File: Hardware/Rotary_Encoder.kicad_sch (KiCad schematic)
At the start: 10 parts, among them SW1 PEC12R-4115F-S0012

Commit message: Clean up custom KiCad libraries
- Clean up the directory structure for KiCad custom libraries.
- Fix paths in KiCad schematic and pcb for symbols, footprints, and
3d models for custom libraries.
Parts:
- SW1: footprint Libs:PEC12R-4115F-S0012 -> Encoder:PEC12R-4115F-S0012
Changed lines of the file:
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@@
   (title_block
     (title "Musical Doorbell")
-    (date "2022-01-06")
-    (rev "B")
+    (date "2022-01-09")
+    (rev "A")
     (company "Michael Lazernik")
   )
@@
     (property "Reference" "SW1" (id 0) (at 143.51 87.1982 0))
     (property "Value" "PEC12R-4115F-S0012" (id 1) (at 143.51 89.5096 0))
-    (property "Footprint" "Libs:PEC12R-4115F-S0012" (id 2) (at 139.7 92.456 0)
+    (property "Footprint" "Encoder:PEC12R-4115F-S0012" (id 2) (at 139.7 92.456 0)
       (effects (font (size 1.27 1.27)) hide)
     )

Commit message: Cleanup custom KiCad libraries
- Delete unneeded/unused files
- Cleanup symbol library files for custom libraries
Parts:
- SW1: symbol PEC12R-4115F-S0012:PEC12R-4115F-S0012 -> Doorbell_Encoder:PEC12R-4115F-S0012
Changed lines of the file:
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@@
     (effects (font (size 1.27 1.27)) (justify left))
   )
-  (symbol (lib_id "PEC12R-4115F-S0012:PEC12R-4115F-S0012") (at 143.51 96.52 0) (unit 1)
+  (symbol (lib_id "Doorbell_Encoder:PEC12R-4115F-S0012") (at 143.51 96.52 0) (unit 1)
     (in_bom yes) (on_board yes)
     (property "Reference" "SW1" (id 0) (at 143.51 87.1982 0))

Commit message: Switch to local libraries for KiCad schematic
- Move all KiCad schematic symbols into local libraries
- Fix KiCad schematic library links to point to local libraries
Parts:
- C33, C34, C35: symbol Device:C_Small -> Doorbell_Capacitor:C_Small
- R26, R27, R28, R29, R30, R31: symbol Device:R_Small -> Doorbell_Resistor:R_Small
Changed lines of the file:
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@@
     (pin "MP")
   )
-  (symbol (lib_id "Device:R_Small") (at 128.27 83.82 0) (unit 1)
+  (symbol (lib_id "Doorbell_Resistor:R_Small") (at 128.27 83.82 0) (unit 1)
     (in_bom yes) (on_board yes)
     (property "Reference" "R28" (id 0) (at 129.7686 82.6516 0)
@@
     (pin "2")
   )
-  (symbol (lib_id "Device:R_Small") (at 123.19 101.6 90) (unit 1)
+  (symbol (lib_id "Doorbell_Resistor:R_Small") (at 123.19 101.6 90) (unit 1)
     (in_bom yes) (on_board yes)
     (property "Reference" "R27" (id 0) (at 123.19 96.6216 90))
@@
     (pin "2")
   )
-  (symbol (lib_id "Device:R_Small") (at 123.19 91.44 270) (unit 1)
+  (symbol (lib_id "Doorbell_Resistor:R_Small") (at 123.19 91.44 270) (unit 1)
     (in_bom yes) (on_board yes)
     (property "Reference" "R26" (id 0) (at 123.19 86.4616 90))
@@
     (pin "2")
   )
-  (symbol (lib_id "Device:R_Small") (at 128.27 109.22 0) (unit 1)
+  (symbol (lib_id "Doorbell_Resistor:R_Small") (at 128.27 109.22 0) (unit 1)
     (in_bom yes) (on_board yes)
     (property "Reference" "R29" (id 0) (at 129.7686 108.0516 0)
@@
     (pin "2")
   )
-  (symbol (lib_id "Device:C_Small") (at 130.81 116.84 0) (unit 1)
+  (symbol (lib_id "Doorbell_Capacitor:C_Small") (at 130.81 116.84 0) (unit 1)
     (in_bom yes) (on_board yes)
     (property "Reference" "C34" (id 0) (at 133.1468 115.6716 0)
@@
     (pin "2")
   )
-  (symbol (lib_id "Device:C_Small") (at 130.81 73.66 0) (unit 1)
+  (symbol (lib_id "Doorbell_Capacitor:C_Small") (at 130.81 73.66 0) (unit 1)
     (in_bom yes) (on_board yes)
     (property "Reference" "C33" (id 0) (at 133.1468 72.4916 0)
@@
     (pin "2")
   )
-  (symbol (lib_id "power:GND") (at 143.51 71.12 0) (unit 1)
+  (symbol (lib_id "Doorbell_Power:GND") (at 143.51 71.12 0) (unit 1)
     (in_bom yes) (on_board yes)
     (property "Reference" "#PWR051" (id 0) (at 143.51 77.47 0)
@@
     (pin "1")
   )
-  (symbol (lib_id "power:GND") (at 130.81 121.92 0) (unit 1)
+  (symbol (lib_id "Doorbell_Power:GND") (at 130.81 121.92 0) (unit 1)
     (in_bom yes) (on_board yes)
     (property "Reference" "#PWR050" (id 0) (at 130.81 128.27 0)
@@
     (pin "1")
   )
-  (symbol (lib_id "Device:R_Small") (at 165.1 93.98 270) (unit 1)
+  (symbol (lib_id "Doorbell_Resistor:R_Small") (at 165.1 93.98 270) (unit 1)
     (in_bom yes) (on_board yes)
     (property "Reference" "R31" (id 0) (at 165.1 89.0016 90))
@@
     (pin "2")
   )
-  (symbol (lib_id "Device:R_Small") (at 157.48 88.9 0) (unit 1)
+  (symbol (lib_id "Doorbell_Resistor:R_Small") (at 157.48 88.9 0) (unit 1)
     (in_bom yes) (on_board yes)
     (property "Reference" "R30" (id 0) (at 158.9786 87.7316 0)
@@
     (pin "2")
   )
-  (symbol (lib_id "Device:C_Small") (at 170.18 99.06 0) (unit 1)
+  (symbol (lib_id "Doorbell_Capacitor:C_Small") (at 170.18 99.06 0) (unit 1)
     (in_bom yes) (on_board yes)
     (property "Reference" "C35" (id 0) (at 172.5168 97.8916 0)
@@
     (pin "2")
   )
-  (symbol (lib_id "power:GND") (at 161.29 109.22 0) (unit 1)
+  (symbol (lib_id "Doorbell_Power:GND") (at 161.29 109.22 0) (unit 1)
     (in_bom yes) (on_board yes)
     (property "Reference" "#PWR052" (id 0) (at 161.29 115.57 0)

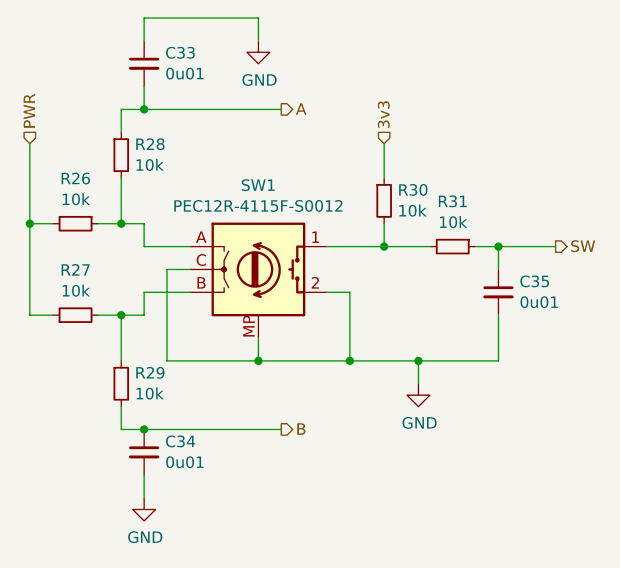
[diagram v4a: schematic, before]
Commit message: Bump to board revision B
- Redesign low battery circuit
	- Replace comparator with PMIC
	- Utilize LED Driver IC
	- Remove unneeded 2.5v voltage reference
- Reroute some signals onto wkup/external interrupt pins
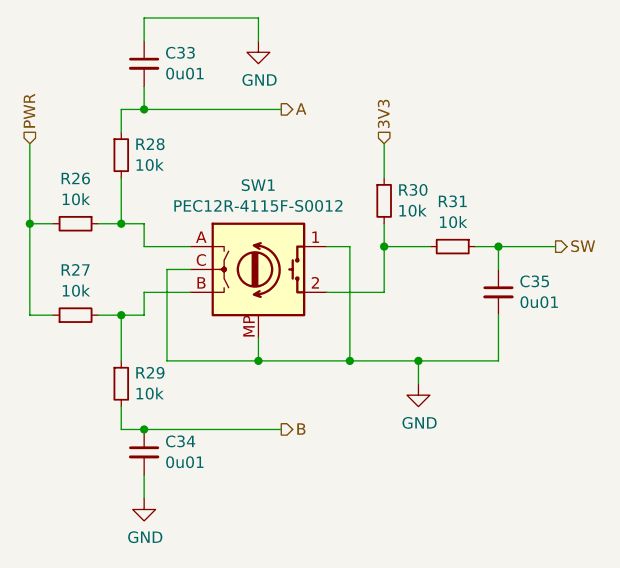
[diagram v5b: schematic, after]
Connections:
- net GND: now also SW1.1; no longer SW1.2
- net at R30.2, R31.2: now also SW1.2; no longer SW1.1
- net 3v3 renamed 3V3
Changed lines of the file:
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@@
   (title_block
     (title "Musical Doorbell")
-    (date "2022-01-11")
-    (rev "A")
+    (date "2022-02-25")
+    (rev "B")
     (company "Michael Lazernik")
+  )
+  (junction (at 153.67 106.68) (diameter 0) (color 0 0 0 0)
   )
   (junction (at 118.11 91.44) (diameter 0) (color 0 0 0 0)
@@
   (junction (at 128.27 91.44) (diameter 0) (color 0 0 0 0)
   )
+  (junction (at 157.48 93.98) (diameter 0) (color 0 0 0 0)
+  )
   (junction (at 170.18 93.98) (diameter 0) (color 0 0 0 0)
   )
   (junction (at 128.27 101.6) (diameter 0) (color 0 0 0 0)
   )
-  (junction (at 157.48 93.98) (diameter 0) (color 0 0 0 0)
-  )
   (junction (at 130.81 78.74) (diameter 0) (color 0 0 0 0)
-  )
-  (junction (at 153.67 106.68) (diameter 0) (color 0 0 0 0)
   )
   (junction (at 143.51 106.68) (diameter 0) (color 0 0 0 0)
@@
     (stroke (width 0) (type default) (color 0 0 0 0))
   )
-  (wire (pts (xy 130.81 101.6) (xy 128.27 101.6))
+  (wire (pts (xy 153.67 93.98) (xy 153.67 106.68))
     (stroke (width 0) (type default) (color 0 0 0 0))
   )
-  (wire (pts (xy 151.13 93.98) (xy 157.48 93.98))
+  (wire (pts (xy 151.13 93.98) (xy 153.67 93.98))
+    (stroke (width 0) (type default) (color 0 0 0 0))
+  )
+  (wire (pts (xy 130.81 101.6) (xy 128.27 101.6))
     (stroke (width 0) (type default) (color 0 0 0 0))
   )
@@
     (stroke (width 0) (type default) (color 0 0 0 0))
   )
-  (wire (pts (xy 153.67 99.06) (xy 153.67 106.68))
+  (wire (pts (xy 128.27 114.3) (xy 130.81 114.3))
     (stroke (width 0) (type default) (color 0 0 0 0))
   )
-  (wire (pts (xy 128.27 114.3) (xy 130.81 114.3))
+  (wire (pts (xy 157.48 93.98) (xy 157.48 99.06))
     (stroke (width 0) (type default) (color 0 0 0 0))
   )
@@
     (stroke (width 0) (type default) (color 0 0 0 0))
   )
-  (wire (pts (xy 161.29 106.68) (xy 153.67 106.68))
-    (stroke (width 0) (type default) (color 0 0 0 0))
-  )
   (wire (pts (xy 135.89 96.52) (xy 133.35 96.52))
     (stroke (width 0) (type default) (color 0 0 0 0))
@@
     (stroke (width 0) (type default) (color 0 0 0 0))
   )
+  (wire (pts (xy 153.67 106.68) (xy 161.29 106.68))
+    (stroke (width 0) (type default) (color 0 0 0 0))
+  )
   (wire (pts (xy 120.65 101.6) (xy 118.11 101.6))
     (stroke (width 0) (type default) (color 0 0 0 0))
@@
     (stroke (width 0) (type default) (color 0 0 0 0))
   )
-  (wire (pts (xy 151.13 99.06) (xy 153.67 99.06))
+  (wire (pts (xy 151.13 99.06) (xy 157.48 99.06))
     (stroke (width 0) (type default) (color 0 0 0 0))
   )
@@
     (effects (font (size 1.27 1.27)) (justify left))
   )
-  (hierarchical_label "3v3" (shape input) (at 157.48 82.55 90)
+  (hierarchical_label "3V3" (shape input) (at 157.48 82.55 90)
     (effects (font (size 1.27 1.27)) (justify left))
   )
